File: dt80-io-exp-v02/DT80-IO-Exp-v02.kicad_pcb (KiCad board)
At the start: 2 copper layers, 200 x 120 mm, 39 parts, among them J1 12V_IN, J10 DI2_IN, J11 UNI_A_V_mV_TC, J12 UNI_B_V_mV_TC, J13 4_20mA_LOOP, J14 RTD_PT100_PT1000, J15 SDI12_SENSOR, J16 RS485_MODBUS_SENSOR, J17 I2C_QWIIC_SENSOR, J18 1WIRE_SENSOR, J19 PULSE_FREQ_COUNT, J2 DT80_RS485, J3 AI1, J4 AI2, J5 AI3, J6 AI4, J7 REL1_OUT, J8 REL2_OUT, J9 DI1_IN, Q1 TLP281_DI1, Q2 TLP281_DI2, SW1 Modbus_ADDR, U1 MAX485, U2 ESP32-WROOM-32, U3 ADS1115, U4 ULN2003, U5 MP1584 12V-5V, U6 AMS1117-3.3

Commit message: Add RTD BP loop and field protection frontends
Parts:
- added C4: 100nF, Capacitor_SMD:C_0603_1608Metric, F.Cu at (154.0, 51.0)
- added C5: 1uF, Capacitor_SMD:C_0603_1608Metric, F.Cu at (154.0, 55.0)
- added C6: 100nF BP_FILTER, Capacitor_SMD:C_0603_1608Metric, F.Cu at (180.0, 42.0)
- added C7: 10nF PULSE_FILTER, Capacitor_SMD:C_0603_1608Metric, F.Cu at (172.0, 108.0)
- added D1: TVS BP_IN, Diode_SMD:D_SOD-323, F.Cu at (166.0, 42.0)
- added D2: TVS RS485_A, Diode_SMD:D_SOD-323, F.Cu at (164.0, 85.0)
- added D3: TVS RS485_B, Diode_SMD:D_SOD-323, F.Cu at (168.0, 85.0)
- added D4: TVS SDI12, Diode_SMD:D_SOD-323, F.Cu at (176.0, 72.0)
- added D5: TVS PULSE, Diode_SMD:D_SOD-323, F.Cu at (180.0, 108.0)
- added R10: 165R 0.1% BP_SHUNT, Resistor_SMD:R_0603_1608Metric, F.Cu at (172.0, 42.0)
- added R11: 100R ADC_FILTER, Resistor_SMD:R_0603_1608Metric, F.Cu at (176.0, 42.0)
- added R12: 120R RS485_TERM DNP, Resistor_SMD:R_0603_1608Metric, F.Cu at (158.0, 88.0)
- added R13: 100k PULSE_PULLDOWN, Resistor_SMD:R_0603_1608Metric, F.Cu at (164.0, 108.0)
- added R9: 430R 0.1%, Resistor_SMD:R_0603_1608Metric, F.Cu at (178.0, 56.0)
- added U7: MAX31865, Package_SO:TSSOP-20_4.4x6.5mm_P0.65mm, F.Cu at (166.0, 58.0)
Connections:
- J13 pad 2: AI3 -> BP_LOOP_IN
- J14 pad 1: (no net) -> RTD_FORCE+
- J14 pad 2: (no net) -> RTD_SENSE+
- J14 pad 3: (no net) -> RTD_SENSE-
- J14 pad 4: (no net) -> RTD_FORCE-
- U2 pad 10: (no net) -> ADDR0
- U2 pad 11: (no net) -> ADDR1
- U2 pad 12: (no net) -> ADDR2
- U2 pad 29: REL1_CTRL -> RTD_CS
- U2 pad 30: REL2_CTRL -> RTD_SCK
- U2 pad 31: (no net) -> RTD_MISO
- U2 pad 37: (no net) -> RTD_MOSI
- U2 pad 8: (no net) -> REL1_CTRL
- U2 pad 9: (no net) -> REL2_CTRL
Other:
- board text added: "BP 4-20mA: 165R SHUNT + FILTER"
- board text added: "MAX31865 PT100 FRONTEND"
- board text added: "PULSE TVS + FILTER"
- board text added: "RS485 TVS + 120R TERM DNP"

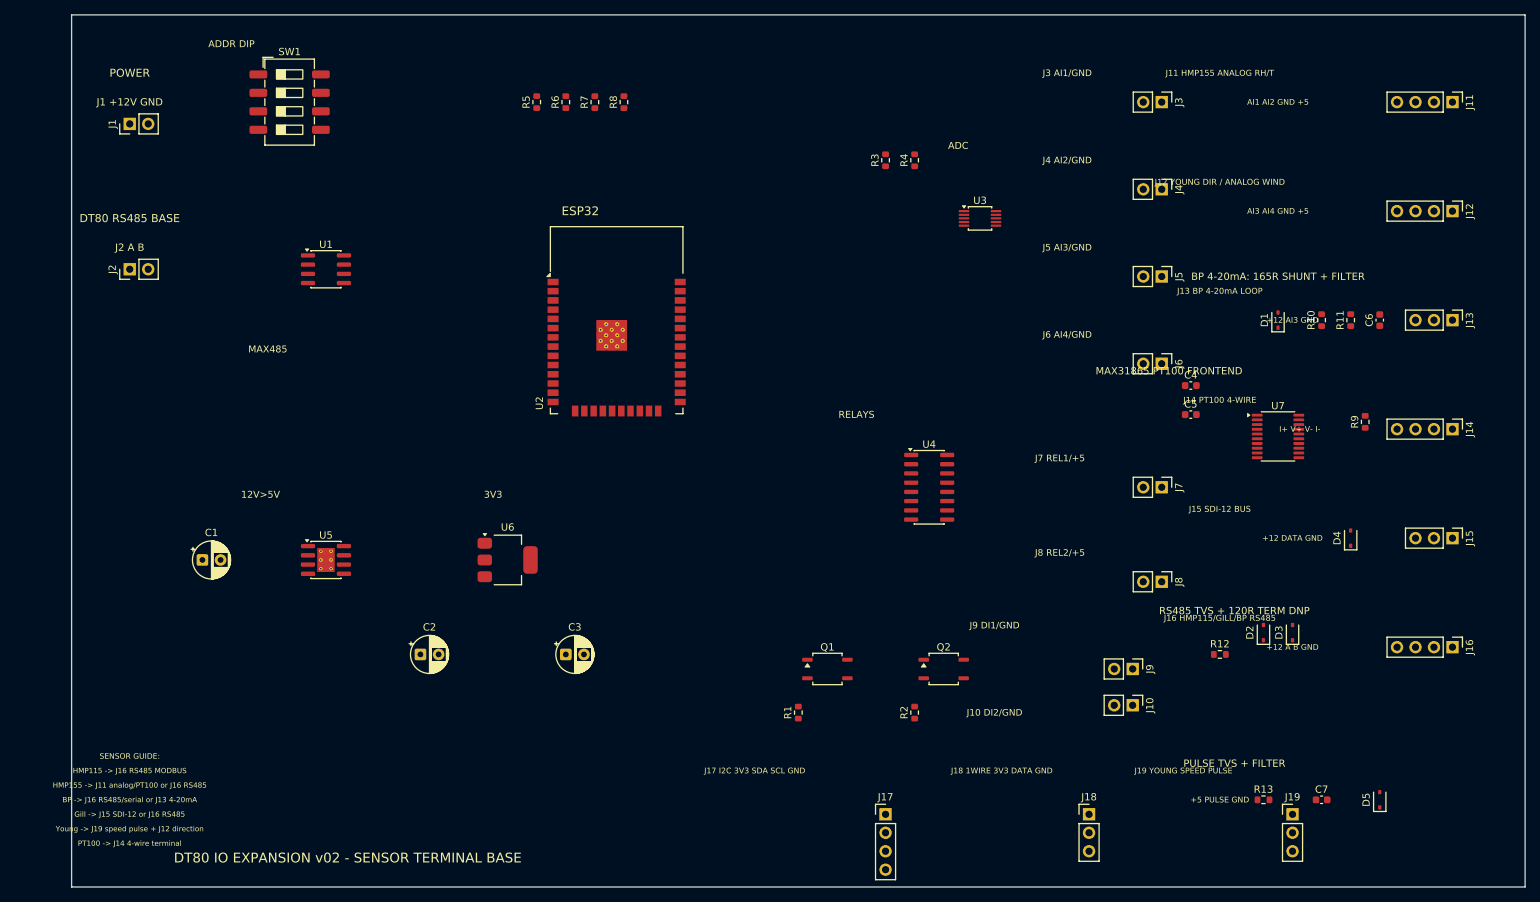
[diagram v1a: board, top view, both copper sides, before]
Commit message: Clean PCB sensor silkscreen labels
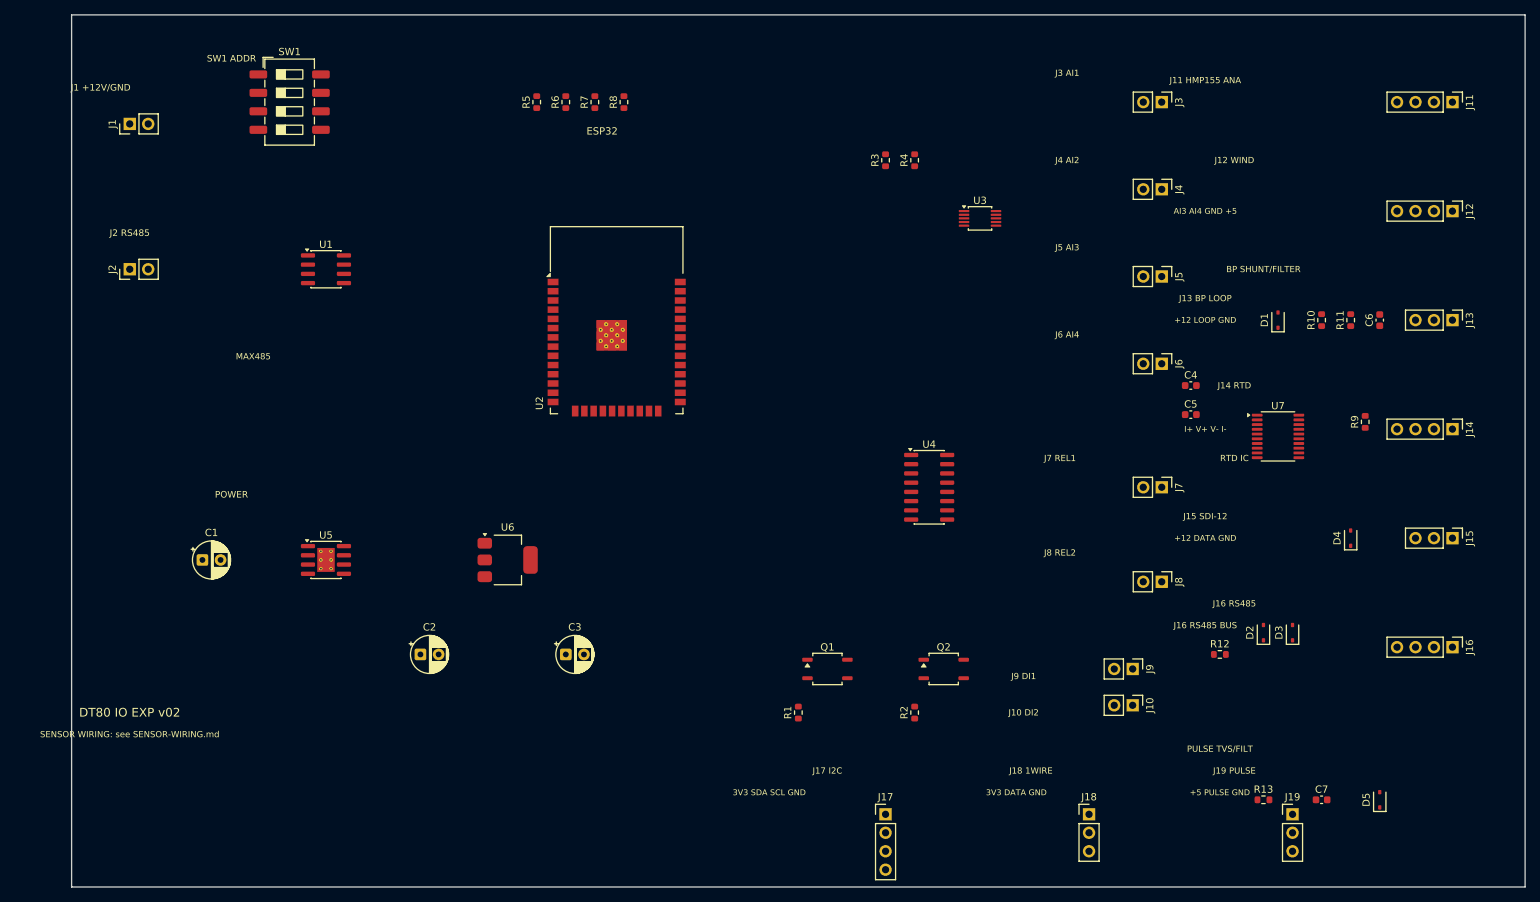
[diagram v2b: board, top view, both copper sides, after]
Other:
- board text added: "+12 LOOP GND"
- board text added: "3V3 DATA GND"
- board text added: "3V3 SDA SCL GND"
- board text added: "BP SHUNT/FILTER"
- board text added: "DT80 IO EXP v02"
- board text added: "J1 +12V/GND"
- board text added: "J10 DI2"
- board text added: "J11 HMP155 ANA"
- board text added: "J12 WIND"
- board text added: "J13 BP LOOP"
- board text added: "J14 RTD"
- board text added: "J15 SDI-12"
- board text added: "J16 RS485"
- board text added: "J16 RS485 BUS"
- board text added: "J17 I2C"
- board text added: "J18 1WIRE"
- board text added: "J19 PULSE"
- board text added: "J2 RS485"
- board text added: "J3 AI1"
- board text added: "J4 AI2"
- board text added: "J5 AI3"
- board text added: "J6 AI4"
- board text added: "J7 REL1"
- board text added: "J8 REL2"
- board text added: "J9 DI1"
- board text added: "PULSE TVS/FILT"
- board text added: "RTD IC"
- board text added: "SENSOR WIRING: see SENSOR-WIRING.md"
- board text added: "SW1 ADDR"
- board text removed: "+12 A B GND"
- board text removed: "+12 AI3 GND"
- board text removed: "12V>5V"
- board text removed: "3V3"
- board text removed: "ADC"
- board text removed: "ADDR DIP"
- board text removed: "AI1 AI2 GND +5"
- board text removed: "BP -> J16 RS485/serial or J13 4-20mA"
- board text removed: "BP 4-20mA: 165R SHUNT + FILTER"
- board text removed: "DT80 IO EXPANSION v02 - SENSOR TERMINAL BASE"
- board text removed: "DT80 RS485 BASE"
- board text removed: "Gill -> J15 SDI-12 or J16 RS485"
- board text removed: "HMP115 -> J16 RS485 MODBUS"
- board text removed: "HMP155 -> J11 analog/PT100 or J16 RS485"
- board text removed: "J1 +12V GND"
- board text removed: "J10 DI2/GND"
- board text removed: "J11 HMP155 ANALOG RH/T"
- board text removed: "J12 YOUNG DIR / ANALOG WIND"
- board text removed: "J13 BP 4-20mA LOOP"
- board text removed: "J14 PT100 4-WIRE"
- board text removed: "J15 SDI-12 BUS"
- board text removed: "J16 HMP115/GILL/BP RS485"
- board text removed: "J17 I2C 3V3 SDA SCL GND"
- board text removed: "J18 1WIRE 3V3 DATA GND"
- board text removed: "J19 YOUNG SPEED PULSE"
- board text removed: "J2 A B"
- board text removed: "J3 AI1/GND"
- board text removed: "J4 AI2/GND"
- board text removed: "J5 AI3/GND"
- board text removed: "J6 AI4/GND"
- board text removed: "J7 REL1/+5"
- board text removed: "J8 REL2/+5"
- board text removed: "J9 DI1/GND"
- board text removed: "MAX31865 PT100 FRONTEND"
- board text removed: "PT100 -> J14 4-wire terminal"
- board text removed: "PULSE TVS + FILTER"
- board text removed: "RELAYS"
- board text removed: "RS485 TVS + 120R TERM DNP"
- board text removed: "SENSOR GUIDE:"
- board text removed: "Young -> J19 speed pulse + J12 direction"

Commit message: Add component net legend on fabrication layer
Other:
- board text added: "D1-D5: TVS field protection"
- board text added: "J11 HMP analog: AI1 AI2 GND +5"
- board text added: "J12 Wind analog: AI3 AI4 GND +5"
- board text added: "J13 BP loop: +12 BP_LOOP GND"
- board text added: "J14 PT100: I+ V+ V- I-"
- board text added: "J15 SDI12: +12 DATA GND"
- board text added: "J16 RS485 bus: +12 A B GND"
- board text added: "LEGEND: COMPONENT TYPE / KEY NETS (F.Fab)"
- board text added: "R10 165R: BP 4-20mA shunt"
- board text added: "R12 120R: RS485 termination DNP"
- board text added: "R13/C7: Young pulse filter"
- board text added: "U1 MAX485: DT80/J16 RS485 A/B"
- board text added: "U2 ESP32: SPI/I2C/RS485/GPIO"
- board text added: "U3 ADS1115: AI1-AI4 analog inputs"
- board text added: "U4 ULN2003: REL1/REL2 drivers"
- board text added: "U7 MAX31865: PT100 SPI -> GPIO5/18/19/23"
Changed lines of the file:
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@@
+		)
+	)
+	(gr_text "LEGEND: COMPONENT TYPE / KEY NETS (F.Fab)"
+		(at 6 78 0)
+		(layer "F.Fab")
+		(effects
+			(font
+				(size 0.85 0.85)
+				(thickness 0.1)
+			)
+		)
+	)
+	(gr_text "U2 ESP32: SPI/I2C/RS485/GPIO"
+		(at 6 80 0)
+		(layer "F.Fab")
+		(effects
+			(font
+				(size 0.85 0.85)
+				(thickness 0.1)
+			)
+		)
+	)
+	(gr_text "U7 MAX31865: PT100 SPI -> GPIO5/18/19/23"
+		(at 6 82 0)
+		(layer "F.Fab")
+		(effects
+			(font
+				(size 0.85 0.85)
+				(thickness 0.1)
+			)
+		)
+	)
+	(gr_text "U3 ADS1115: AI1-AI4 analog inputs"
+		(at 6 84 0)
+		(layer "F.Fab")
+		(effects
+			(font
+				(size 0.85 0.85)
+				(thickness 0.1)
+			)
+		)
+	)
+	(gr_text "U1 MAX485: DT80/J16 RS485 A/B"
+		(at 6 86 0)
+		(layer "F.Fab")
+		(effects
+			(font
+				(size 0.85 0.85)
+				(thickness 0.1)
+			)
+		)
+	)
+	(gr_text "U4 ULN2003: REL1/REL2 drivers"
+		(at 6 88 0)
+		(layer "F.Fab")
+		(effects
+			(font
+				(size 0.85 0.85)
+				(thickness 0.1)
+			)
+		)
+	)
+	(gr_text "J11 HMP analog: AI1 AI2 GND +5"
+		(at 6 90 0)
+		(layer "F.Fab")
+		(effects
+			(font
+				(size 0.85 0.85)
+				(thickness 0.1)
+			)
+		)
+	)
+	(gr_text "J12 Wind analog: AI3 AI4 GND +5"
+		(at 6 92 0)
+		(layer "F.Fab")
+		(effects
+			(font
+				(size 0.85 0.85)
+				(thickness 0.1)
+			)
+		)
+	)
+	(gr_text "J13 BP loop: +12 BP_LOOP GND"
+		(at 6 94 0)
+		(layer "F.Fab")
+		(effects
+			(font
+				(size 0.85 0.85)
+				(thickness 0.1)
+			)
+		)
+	)
+	(gr_text "J14 PT100: I+ V+ V- I-"
+		(at 6 96 0)
+		(layer "F.Fab")
+		(effects
+			(font
+				(size 0.85 0.85)
+				(thickness 0.1)
+			)
+		)
+	)
+	(gr_text "J15 SDI12: +12 DATA GND"
+		(at 6 98 0)
+		(layer "F.Fab")
+		(effects
+			(font
+				(size 0.85 0.85)
+				(thickness 0.1)
+			)
+		)
+	)
+	(gr_text "J16 RS485 bus: +12 A B GND"
+		(at 6 100 0)
+		(layer "F.Fab")
+		(effects
+			(font
+				(size 0.85 0.85)
+				(thickness 0.1)
+			)
+		)
+	)
+	(gr_text "R10 165R: BP 4-20mA shunt"
+		(at 6 102 0)
+		(layer "F.Fab")
+		(effects
+			(font
+				(size 0.85 0.85)
+				(thickness 0.1)
+			)
+		)
+	)
+	(gr_text "R12 120R: RS485 termination DNP"
+		(at 6 104 0)
+		(layer "F.Fab")
+		(effects
+			(font
+				(size 0.85 0.85)
+				(thickness 0.1)
+			)
+		)
+	)
+	(gr_text "D1-D5: TVS field protection"
+		(at 6 106 0)
+		(layer "F.Fab")
+		(effects
+			(font
+				(size 0.85 0.85)
+				(thickness 0.1)
+			)
+		)
+	)
+	(gr_text "R13/C7: Young pulse filter"
+		(at 6 108 0)
+		(layer "F.Fab")
+		(effects
+			(font
+				(size 0.85 0.85)
+				(thickness 0.1)
+			)
 		)
 	)

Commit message: Finalize DT80 v02 routing and fabrication package
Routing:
- net GND: track 0.00 -> 826.1 mm, vias 0 -> 3
- net +3V3: track 0.00 -> 364.8 mm, vias 0 -> 4
- net +5V: track 0.00 -> 339.5 mm, vias 0 -> 3
- net 12V_IN: track 0.00 -> 296.9 mm
- net RS485_A: track 0.00 -> 238.5 mm, vias 0 -> 2
- net RS485_B: track 0.00 -> 222.5 mm, vias 0 -> 2
- net I2C_SDA: track 0.00 -> 156.0 mm, vias 0 -> 3
- net PULSE_COUNT: track 0.00 -> 153.6 mm, vias 0 -> 1
- net I2C_SCL: track 0.00 -> 141.7 mm, vias 0 -> 3
- net SDI12_DATA: track 0.00 -> 116.9 mm
- net ADDR1: track 0.00 -> 103.5 mm, vias 0 -> 2
- net ONEWIRE_DATA: track 0.00 -> 100.2 mm, vias 0 -> 1
- net ADDR0: track 0.00 -> 98.3 mm, vias 0 -> 2
- net ADDR2: track 0.00 -> 97.1 mm, vias 0 -> 2
- net RTD_MOSI: track 0.00 -> 87.5 mm
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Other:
- board text added: "J11 HMP ANA"
- board text removed: "+12 DATA GND"
- board text removed: "+12 LOOP GND"
- board text removed: "+5 PULSE GND"
- board text removed: "3V3 DATA GND"
- board text removed: "3V3 SDA SCL GND"
- board text removed: "AI3 AI4 GND +5"
- board text removed: "D1-D5: TVS field protection"
- board text removed: "I+ V+ V- I-"
- board text removed: "J11 HMP analog: AI1 AI2 GND +5"
- board text removed: "J11 HMP155 ANA"
- board text removed: "J12 Wind analog: AI3 AI4 GND +5"
- board text removed: "J13 BP loop: +12 BP_LOOP GND"
- board text removed: "J14 PT100: I+ V+ V- I-"
- board text removed: "J15 SDI12: +12 DATA GND"
- board text removed: "J16 RS485 BUS"
- board text removed: "J16 RS485 bus: +12 A B GND"
- board text removed: "LEGEND: COMPONENT TYPE / KEY NETS (F.Fab)"
- board text removed: "R10 165R: BP 4-20mA shunt"
- board text removed: "R12 120R: RS485 termination DNP"
- board text removed: "R13/C7: Young pulse filter"
- board text removed: "SENSOR WIRING: see SENSOR-WIRING.md"
- board text removed: "U1 MAX485: DT80/J16 RS485 A/B"
- board text removed: "U2 ESP32: SPI/I2C/RS485/GPIO"
- board text removed: "U3 ADS1115: AI1-AI4 analog inputs"
- board text removed: "U4 ULN2003: REL1/REL2 drivers"
- board text removed: "U7 MAX31865: PT100 SPI -> GPIO5/18/19/23"
